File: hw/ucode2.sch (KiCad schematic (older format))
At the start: 14 parts, among them U801 74HC00, U802 74HC590, U803 27C64, U804 27C64, U805 27C64, U806 27C64, U807 74HCT175, U808 74HCT175, U809 74HCT175, U810 74HCT175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

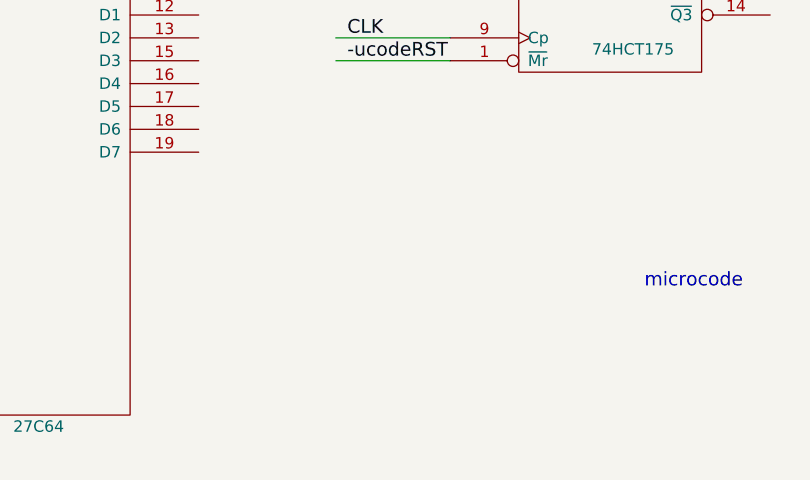
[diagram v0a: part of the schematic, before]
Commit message: add unused gates to ucode2 schematic
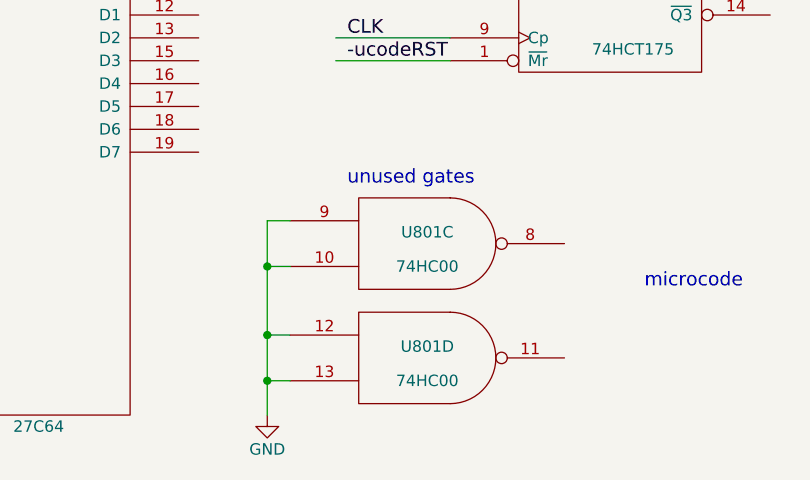
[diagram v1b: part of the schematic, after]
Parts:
- added unit 3 of U801
- added unit 4 of U801
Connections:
- wire segments 181 -> 186
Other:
- note added: "unused gates"
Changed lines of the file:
@@
 $Descr A4 11693 8268
 encoding utf-8
-Sheet 10 10
+Sheet 9 9
 Title ""
 Date ""
@@
 Text Label 5850 5800 0    60   ~ 0
 -ucodeRST
+$Comp
+L 74LS00 U801
+U 3 1 59522853
+P 6200 6600
+F 0 "U801" H 6200 6650 50  0000 C CNN
+F 1 "74HC00" H 6200 6500 50  0000 C CNN
+F 2 "" H 6200 6600 50  0001 C CNN
+F 3 "" H 6200 6600 50  0001 C CNN
+	3    6200 6600
+	1    0    0    -1
+$EndComp
+$Comp
+L 74LS00 U801
+U 4 1 59522859
+P 6200 7100
+F 0 "U801" H 6200 7150 50  0000 C CNN
+F 1 "74HC00" H 6200 7000 50  0000 C CNN
+F 2 "" H 6200 7100 50  0001 C CNN
+F 3 "" H 6200 7100 50  0001 C CNN
+	4    6200 7100
+	1    0    0    -1
+$EndComp
+Wire Wire Line
+	5600 6500 5500 6500
+Wire Wire Line
+	5500 6500 5500 7350
+Wire Wire Line
+	5600 6700 5500 6700
+Connection ~ 5500 6700
+Wire Wire Line
+	5600 7000 5500 7000
+Connection ~ 5500 7000
+Wire Wire Line
+	5600 7200 5500 7200
+Connection ~ 5500 7200
+$Comp
+L GND #PWR?
+U 1 1 59522CEA
+P 5500 7350
+F 0 "#PWR?" H 5500 7100 50  0001 C CNN
+F 1 "GND" H 5500 7200 50  0000 C CNN
+F 2 "" H 5500 7350 50  0001 C CNN
+F 3 "" H 5500 7350 50  0001 C CNN
+	1    5500 7350
+	1    0    0    -1
+$EndComp
+Text Notes 5850 6350 0    60   ~ 0
+unused gates
 $EndSCHEMATC

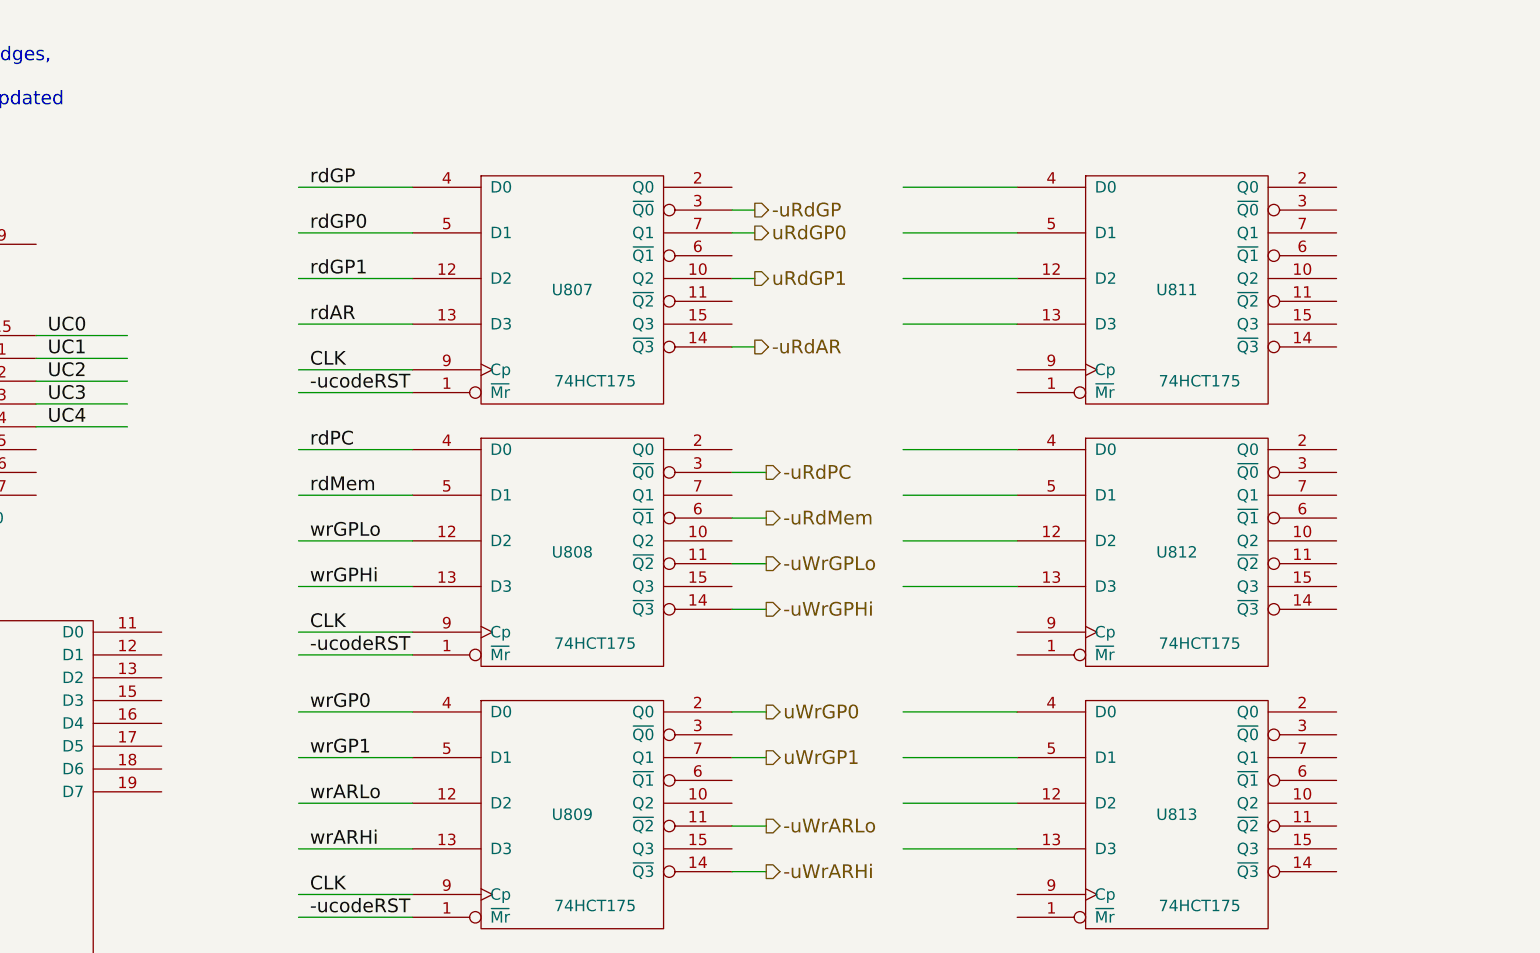
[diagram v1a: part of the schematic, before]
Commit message: make ROM 3 the ALU control ROM
Need to think about how to handle conditional branch
logic (e.g., "end if equal", "end if not equal",
etc.)
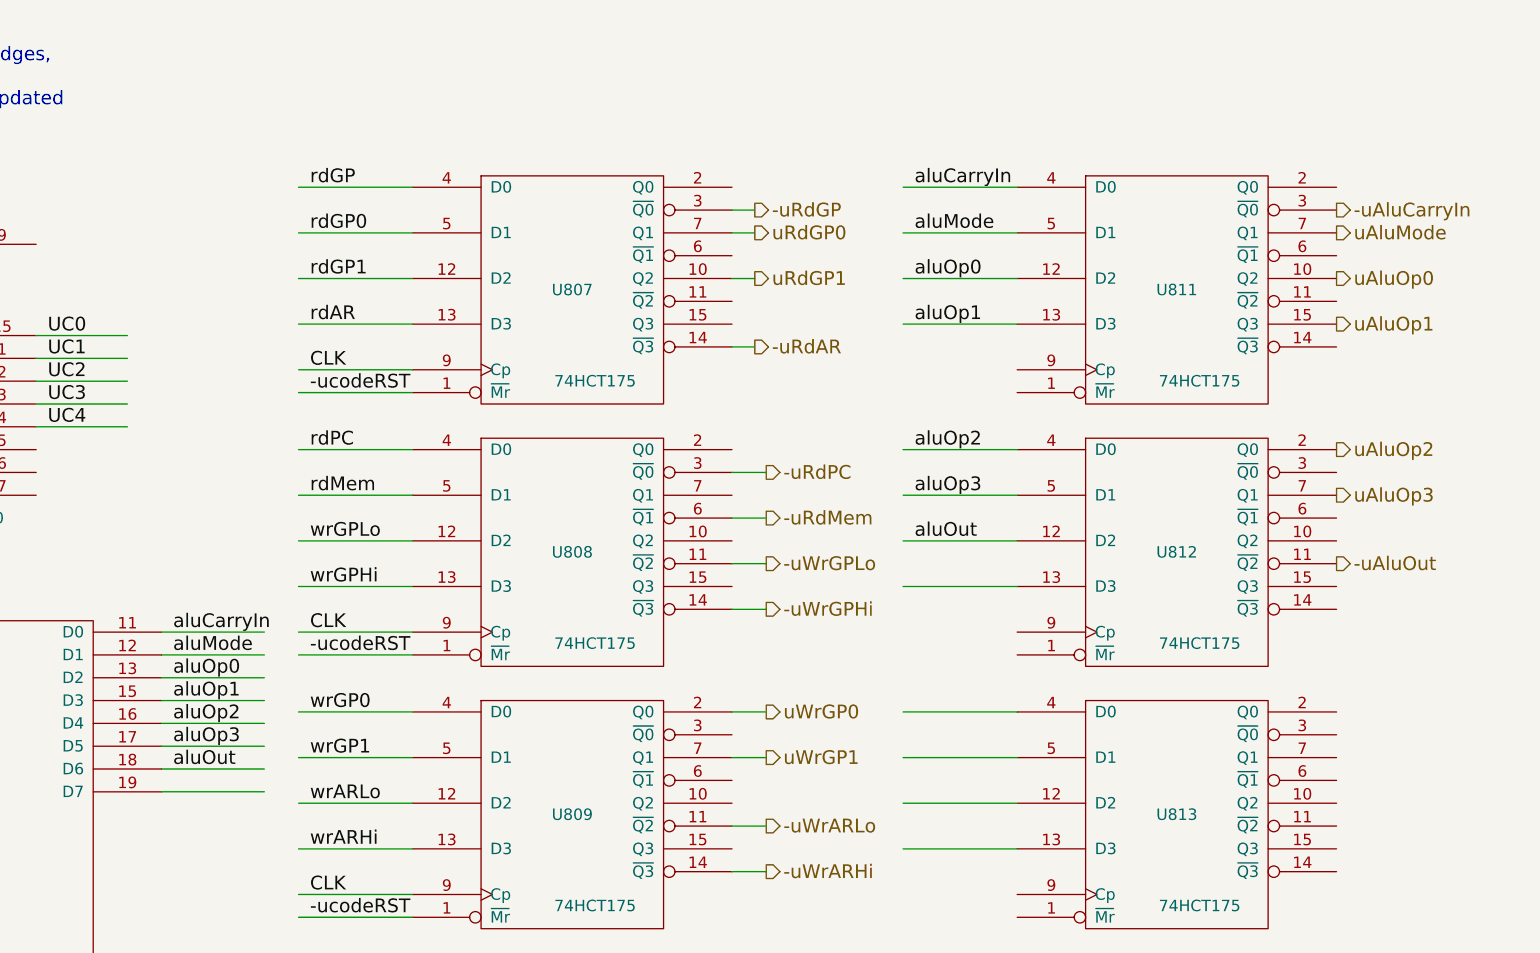
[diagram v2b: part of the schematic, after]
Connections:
- net labels added: -uAluCarryIn, -uAluOut, aluCarryIn, aluMode, aluOp0, aluOp1, aluOp2, aluOp3, aluOut, uAluMode, uAluOp0, uAluOp1, uAluOp2, uAluOp3
- wire segments 186 -> 194
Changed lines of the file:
@@
 Text Notes 5850 6350 0    60   ~ 0
 unused gates
+Wire Wire Line
+	5200 3400 5650 3400
+Wire Wire Line
+	5200 3500 5650 3500
+Wire Wire Line
+	5200 3600 5650 3600
+Wire Wire Line
+	5200 3700 5650 3700
+Wire Wire Line
+	5200 3800 5650 3800
+Wire Wire Line
+	5200 3900 5650 3900
+Wire Wire Line
+	5200 4000 5650 4000
+Wire Wire Line
+	5200 4100 5650 4100
+Text Label 5250 3400 0    60   ~ 0
+aluCarryIn
+Text Label 5250 3500 0    60   ~ 0
+aluMode
+Text Label 5250 3600 0    60   ~ 0
+aluOp0
+Text Label 5250 3700 0    60   ~ 0
+aluOp1
+Text Label 5250 3800 0    60   ~ 0
+aluOp2
+Text Label 5250 3900 0    60   ~ 0
+aluOp3
+Text Label 5250 4000 0    60   ~ 0
+aluOut
+Text Label 8500 1450 0    60   ~ 0
+aluCarryIn
+Text Label 8500 1650 0    60   ~ 0
+aluMode
+Text Label 8500 1850 0    60   ~ 0
+aluOp0
+Text Label 8500 2050 0    60   ~ 0
+aluOp1
+Text Label 8500 2600 0    60   ~ 0
+aluOp2
+Text Label 8500 2800 0    60   ~ 0
+aluOp3
+Text Label 8500 3000 0    60   ~ 0
+aluOut
+Text HLabel 10350 1550 2    60   Output ~ 0
+-uAluCarryIn
+Text HLabel 10350 1650 2    60   Output ~ 0
+uAluMode
+Text HLabel 10350 1850 2    60   Output ~ 0
+uAluOp0
+Text HLabel 10350 2050 2    60   Output ~ 0
+uAluOp1
+Text HLabel 10350 2600 2    60   Output ~ 0
+uAluOp2
+Text HLabel 10350 2800 2    60   Output ~ 0
+uAluOp3
+Text HLabel 10350 3100 2    60   Output ~ 0
+-uAluOut
 $EndSCHEMATC
